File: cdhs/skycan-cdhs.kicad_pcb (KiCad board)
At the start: 2 copper layers, 50 x 50 mm, 50 parts, among them J1 DF9-25P-1V-PLUG, J2 DF9-25P-1V-SOCKET, J3 DF9-25P-1V-PLUG, J4 DF9-25P-1V-SOCKET, P1 CONN_3X2, SW1 SW_PUSH_4_PIN, U1 MSP430F5528IRGCT, U2 MICRO-B_USB, U3 FM24CL04B, U4 SST25VF080B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

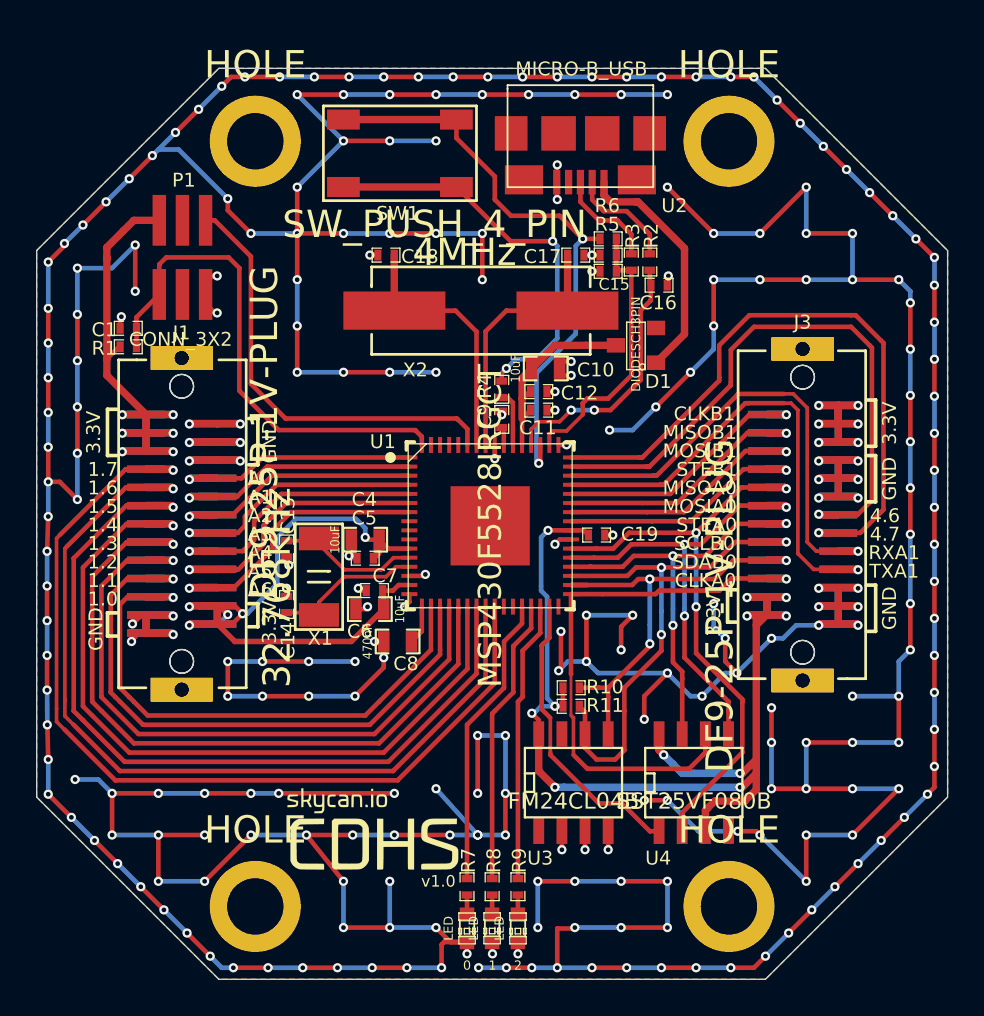
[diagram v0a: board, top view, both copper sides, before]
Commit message: Now CDHS uses only skycan lib Mounting holes connected to gnd
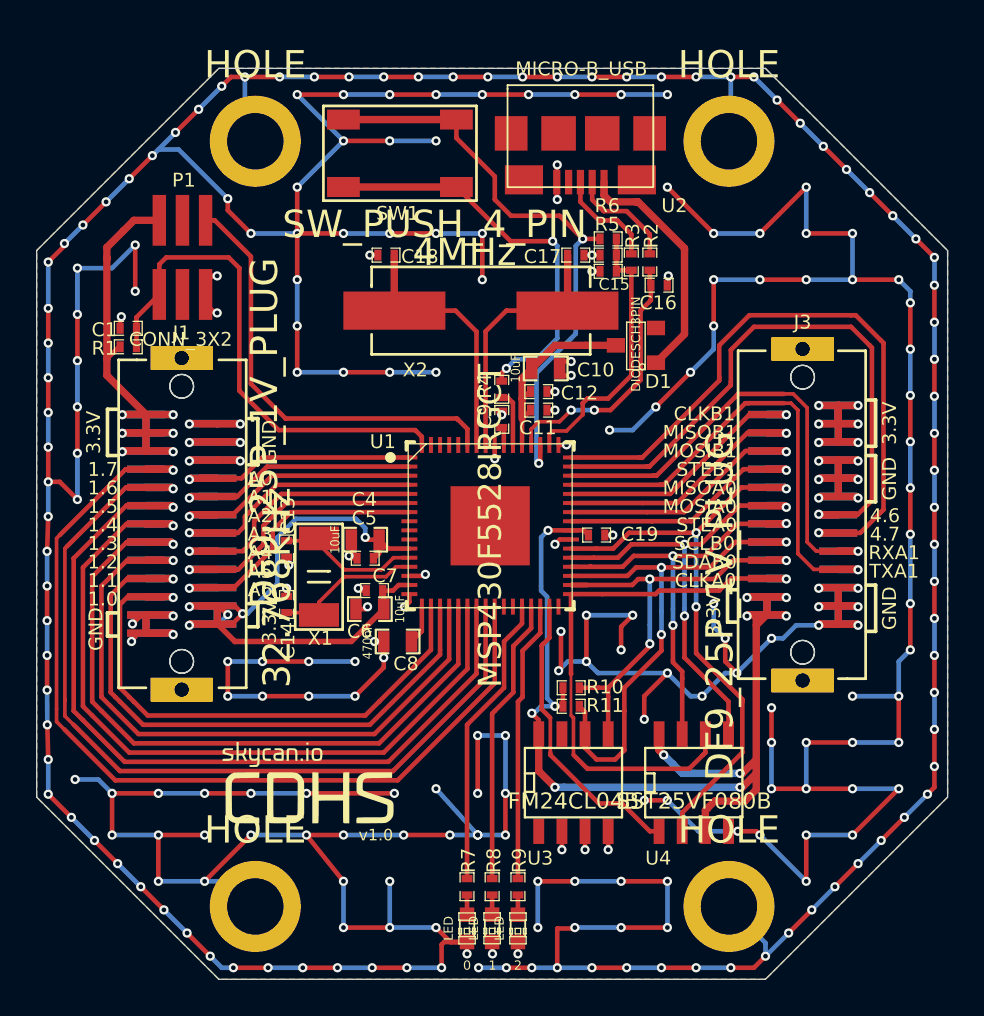
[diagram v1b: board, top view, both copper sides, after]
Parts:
- J1, J3: value DF9-25P-1V-PLUG -> DF9_25P_1V_PLUG
- J2, J4: value DF9-25P-1V-SOCKET -> DF9_25P_1V_SOCKET
- U1: footprint andrew/b3kma -> S-PVQFN-N64
- moved VAL 4.37 mm to (114.6, 128.8)
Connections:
- H1 pad 1: (no net) -> GND
- H2 pad 1: (no net) -> GND
- H3 pad 1: (no net) -> GND
- H4 pad 1: (no net) -> GND
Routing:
- net GND: track 613.3 -> 627.5 mm

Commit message: Updated cdhs silkscreen to v1.1
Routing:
- net GND: track 627.5 -> 630.0 mm, vias 283 -> 284
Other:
- board text added: "v1.1"
- board text removed: "v1.0"
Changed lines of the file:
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@@
     (links 197)
     (no_connects 3)
-    (area 99.987299 89.987299 150.012701 140.012701)
+    (area 99.987299 88.8226 150.012701 140.012701)
     (thickness 1.6)
     (drawings 74)
-    (tracks 1515)
+    (tracks 1517)
     (zones 0)
     (modules 50)
@@
   (layers
     (15 F.Cu signal)
-    (0 B.Cu signal)
+    (0 B.Cu signal hide)
     (16 B.Adhes user)
     (17 F.Adhes user)
@@
   (gr_line (start 103.886 111.252) (end 103.886 108.712) (angle 90) (layer F.SilkS) (width 0.2))
   (gr_line (start 104.394 111.252) (end 103.886 111.252) (angle 90) (layer F.SilkS) (width 0.2))
-  (gr_text v1.0 (at 118.618 132.08) (layer F.SilkS)
+  (gr_text v1.1 (at 118.618 132.08) (layer F.SilkS)
     (effects (font (size 0.635 0.635) (thickness 0.127)))
   )
@@
   (segment (start 128.142 121.256) (end 127.813 121.585) (width 0.254) (layer F.Cu) (net 13))
   (segment (start 127.71937 121.67863) (end 127.813 121.585) (width 0.254) (layer F.Cu) (net 13))
+  (segment (start 121.92 137.16) (end 121.92 134.62) (width 0.254) (layer B.Cu) (net 14))
+  (via (at 121.92 134.62) (size 0.508) (layers F.Cu B.Cu) (net 14))
   (segment (start 111.76 129.794) (end 114.808 129.794) (width 0.254) (layer B.Cu) (net 14))
   (via (at 106.68 129.794) (size 0.508) (layers F.Cu B.Cu) (net 14))

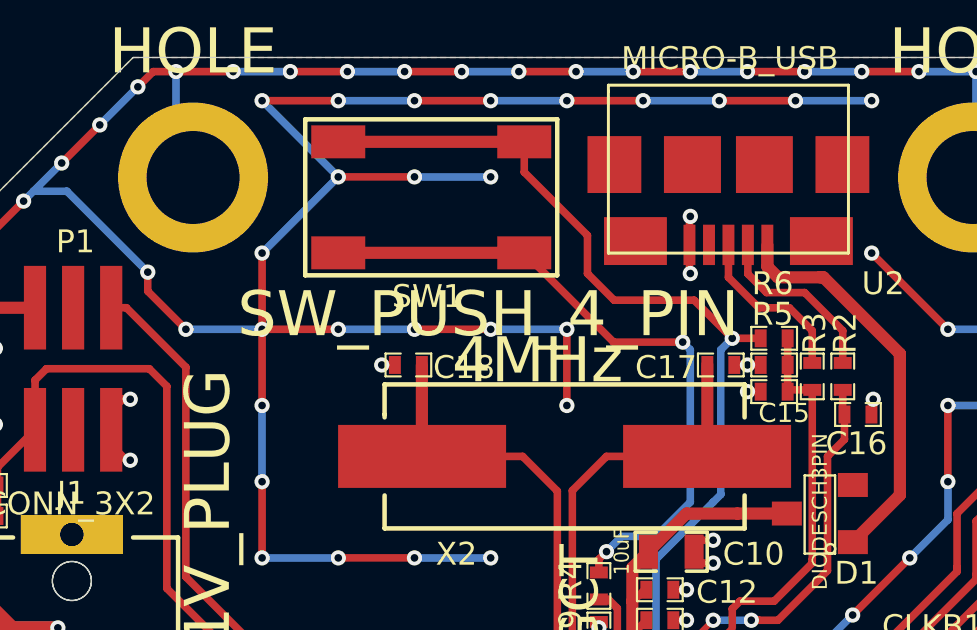
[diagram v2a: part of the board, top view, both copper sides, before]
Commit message: Added Farnell codes and footprints to CDHS schematic
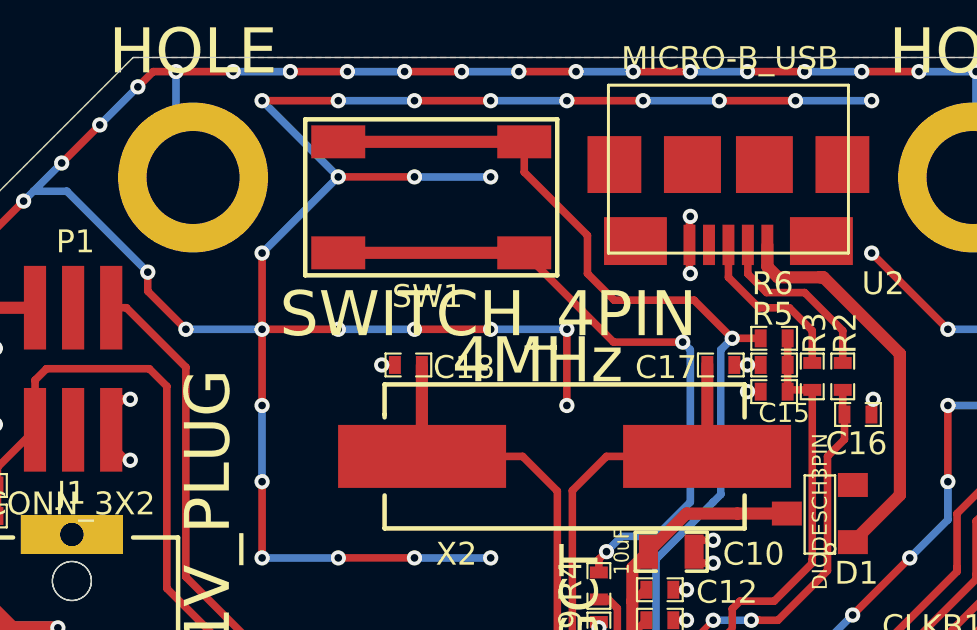
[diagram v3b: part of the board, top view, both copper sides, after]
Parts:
- SW1: value SW_PUSH_4_PIN -> SWITCH_4PIN
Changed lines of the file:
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@@
     (links 197)
     (no_connects 3)
-    (area 99.987299 88.8226 150.012701 140.012701)
+    (area 99.987299 89.987299 150.012701 140.012701)
     (thickness 1.6)
     (drawings 74)
@@
   )
   (setup
-    (last_trace_width 0.254)
+    (last_trace_width 0.1524)
     (user_trace_width 0.2032)
     (user_trace_width 0.254)
@@
   (net 17 LED2)
   (net 18 N-0000014)
-  (net 19 N-0000019)
-  (net 20 N-0000020)
-  (net 21 N-0000021)
-  (net 22 N-0000024)
-  (net 23 N-0000025)
-  (net 24 N-0000026)
-  (net 25 N-0000027)
-  (net 26 N-0000028)
-  (net 27 N-0000031)
-  (net 28 N-0000034)
-  (net 29 N-0000037)
-  (net 30 N-0000039)
-  (net 31 N-0000042)
+  (net 19 N-0000017)
+  (net 20 N-0000018)
+  (net 21 N-0000019)
+  (net 22 N-0000021)
+  (net 23 N-0000022)
+  (net 24 N-0000023)
+  (net 25 N-0000025)
+  (net 26 N-0000026)
+  (net 27 N-0000027)
+  (net 28 N-0000028)
+  (net 29 N-0000033)
+  (net 30 N-0000040)
+  (net 31 N-0000045)
   (net 32 N-0000052)
   (net 33 N-0000053)
@@
     (add_net LED2)
     (add_net N-0000014)
+    (add_net N-0000017)
+    (add_net N-0000018)
     (add_net N-0000019)
-    (add_net N-0000020)
     (add_net N-0000021)
-    (add_net N-0000024)
+    (add_net N-0000022)
+    (add_net N-0000023)
     (add_net N-0000025)
     (add_net N-0000026)
     (add_net N-0000027)
     (add_net N-0000028)
-    (add_net N-0000031)
-    (add_net N-0000034)
-    (add_net N-0000037)
-    (add_net N-0000039)
-    (add_net N-0000042)
+    (add_net N-0000033)
+    (add_net N-0000040)
+    (add_net N-0000045)
     (add_net N-0000052)
     (add_net N-0000053)
@@
     (pad 8 smd rect (at -0.25 4.435961 180) (size 0.878078 0.22)
       (layers F.Cu F.Paste F.Mask)
-      (net 19 N-0000019)
+      (net 19 N-0000017)
     )
     (pad 9 smd rect (at 0.25 4.435961 180) (size 0.878078 0.22)
       (layers F.Cu F.Paste F.Mask)
-      (net 20 N-0000020)
+      (net 20 N-0000018)
     )
     (pad 10 smd rect (at 0.75 4.435961 180) (size 0.878078 0.22)
       (layers F.Cu F.Paste F.Mask)
-      (net 21 N-0000021)
+      (net 21 N-0000019)
     )
     (pad 11 smd rect (at 1.25 4.435961 180) (size 0.878078 0.22)
@@
     (pad 26 smd rect (at 4.435961 -0.75 270) (size 0.878078 0.22)
       (layers F.Cu F.Paste F.Mask)
-      (net 27 N-0000031)
+      (net 31 N-0000045)
     )
     (pad 27 smd rect (at 4.435961 -1.25 270) (size 0.878078 0.22)
       (layers F.Cu F.Paste F.Mask)
-      (net 28 N-0000034)
+      (net 29 N-0000033)
     )
     (pad 28 smd rect (at 4.435961 -1.75 270) (size 0.878078 0.22)
@@
     (pad 32 smd rect (at 4.435961 -3.75 270) (size 0.878078 0.22)
       (layers F.Cu F.Paste F.Mask)
-      (net 29 N-0000037)
+      (net 24 N-0000023)
     )
     (pad 33 smd rect (at 3.75 -4.435961) (size 0.878078 0.22)
@@
     (pad 60 smd rect (at -4.435961 1.75 90) (size 0.878078 0.22)
       (layers F.Cu F.Paste F.Mask)
-      (net 22 N-0000024)
+      (net 22 N-0000021)
     )
     (pad 61 smd rect (at -4.435961 2.25 90) (size 0.878078 0.22)
       (layers F.Cu F.Paste F.Mask)
-      (net 23 N-0000025)
+      (net 23 N-0000022)
     )
     (pad 62 smd rect (at -4.435961 2.75 90) (size 0.878078 0.22)
       (layers F.Cu F.Paste F.Mask)
-      (net 30 N-0000039)
+      (net 27 N-0000027)
     )
     (pad 63 smd rect (at -4.435961 3.25 90) (size 0.878078 0.22)
       (layers F.Cu F.Paste F.Mask)
-      (net 31 N-0000042)
+      (net 30 N-0000040)
     )
     (pad 64 smd rect (at -4.435961 3.75 90) (size 0.878078 0.22)
@@
       (effects (font (size 0.762 0.762) (thickness 0.127)))
     )
-    (fp_text value SW_PUSH_4_PIN (at -1.9 -3.9 180) (layer F.SilkS)
+    (fp_text value SWITCH_4PIN (at -1.9 -3.9 180) (layer F.SilkS)
       (effects (font (size 1.5 1.5) (thickness 0.15)))
     )
@@
     (pad 4 smd rect (at 0.6477 -4.12496 180) (size 0.39878 1.3462)
       (layers F.Cu F.Paste F.Mask)
-      (net 26 N-0000028)
+      (net 28 N-0000028)
       (clearance 0.2032)
     )
@@
     (pad 1 smd rect (at -1.905 2.667) (size 0.59944 1.39954)
       (layers F.Cu F.Paste F.Mask)
-      (net 24 N-0000026)
+      (net 25 N-0000025)
     )
     (pad 7 smd rect (at -0.635 -2.667) (size 0.59944 1.39954)
       (layers F.Cu F.Paste F.Mask)
-      (net 25 N-0000027)
+      (net 26 N-0000026)
     )
     (pad 6 smd rect (at 0.635 -2.667) (size 0.59944 1.39954)
